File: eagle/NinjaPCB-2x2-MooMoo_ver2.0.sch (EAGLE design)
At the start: 75 parts, among them IC1 ANALOGSW_AD_SOT23-6, IC2 NAU7802, Q1 IRLB3813PBF, Q2 CJ2302, Q3 CJ2302, Q4 S9013, Q5 S9013, Q6 S9013, T1 TPTP20R, T2 TPTP20R, T3 TPTP20R, T4 TPTP20R, T5 TPTP20R, T6 TPTP20R, T7 TPTP20R

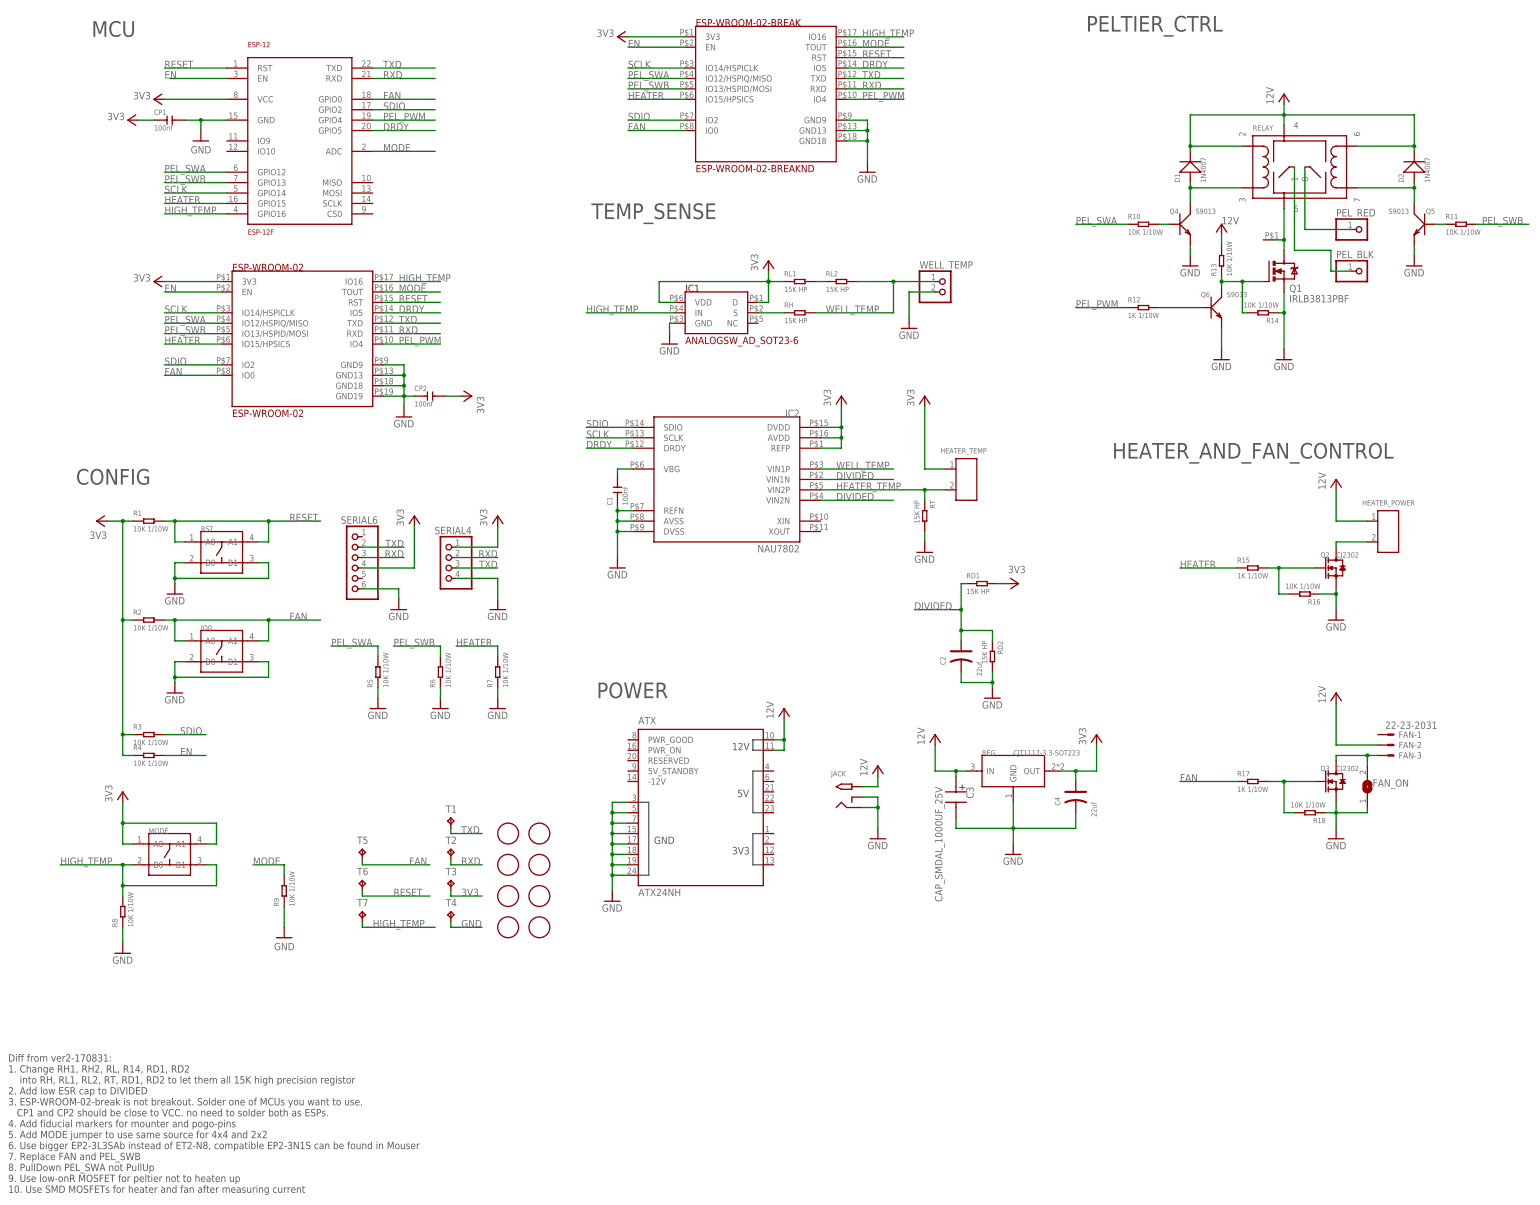
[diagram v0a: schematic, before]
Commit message: panelized NinNin
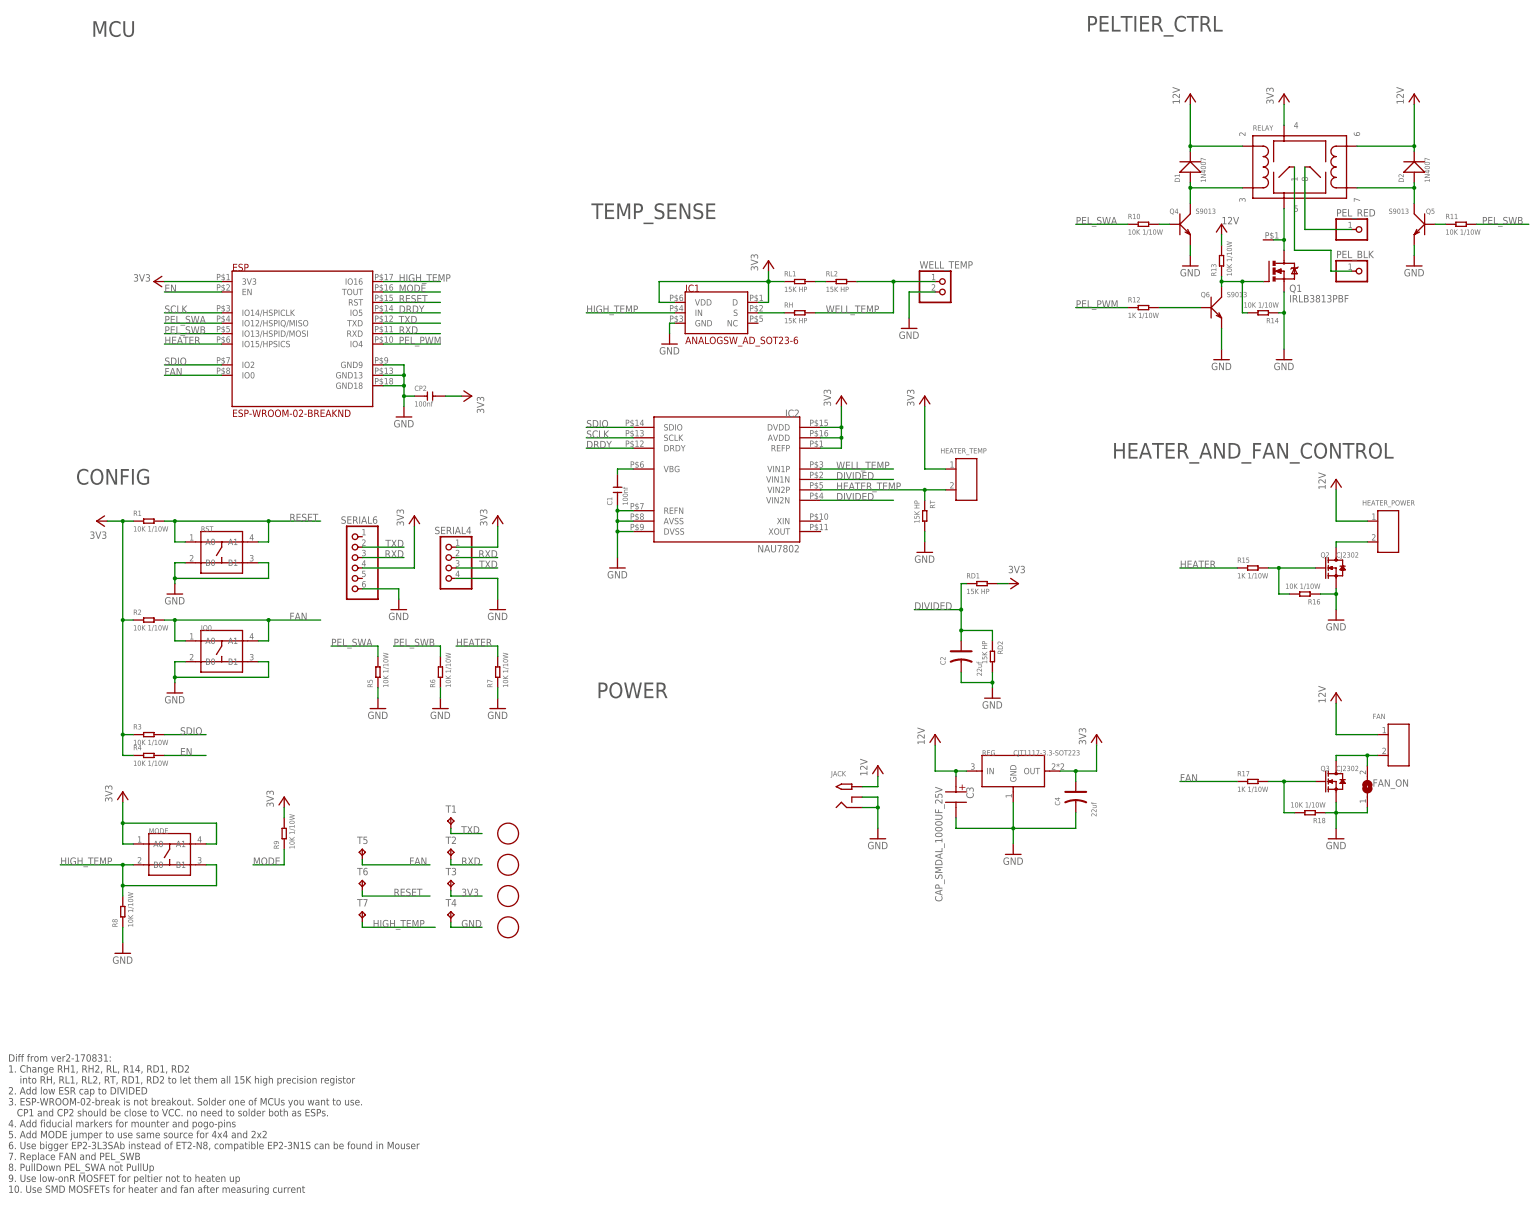
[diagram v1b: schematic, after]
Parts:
- removed ATX: ATX24NH, PCR-Connector:ATX24NH
- removed CP1: 100nf, Seeed-Capacitor:CERAMIC-100NF-50V-10%-X7R(0603)
- removed ESP-12: ESP-12F, Seeed-OPL-2017-01-Sensor-camilo:ESP-12F
- removed ESP-WROOM-02: ESP-WROOM-02, PCR-Module:ESP-WROOM-02
- removed ESP-WROOM-02-BREAK: ESP-WROOM-02-BREAKND, PCR-Module:ESP-WROOM-02-BREAKND
- removed U$10, U$7, U$8, U$9: FIDUCIAL, adafruit:FIDUCIAL
- added ESP: ESP-WROOM-02-BREAKND, PCR-Module:ESP-WROOM-02-BREAKND
- FAN: value 22-23-2031 -> (none); device con-molex:22-23-2031 -> Seeed-Connector:SCREW-TERMINAL-GREEN(2P-3.5)
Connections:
- new net N$9: D1.-, RELAY.2
- net 12V: now also FAN.1; no longer ATX.12V_10, ATX.12V_11, D1.-, FAN-2.S, RELAY.2, RELAY.4
- net 3V3: now also ESP.3V3, R9.2, RELAY.4; no longer CP1.1, ESP-12.VCC, ESP-WROOM-02-BREAK.3V3, ESP-WROOM-02.3V3
- net DRDY: now also ESP.IO5; no longer ESP-12.GPIO5, ESP-WROOM-02-BREAK.IO5, ESP-WROOM-02.IO5
- net EN: now also ESP.EN; no longer ESP-12.EN, ESP-WROOM-02-BREAK.EN, ESP-WROOM-02.EN
- net FAN: now also ESP.IO0; no longer ESP-12.GPIO0, ESP-WROOM-02-BREAK.IO0, ESP-WROOM-02.IO0
- net GND: now also ESP.GND13, ESP.GND18, ESP.GND9; no longer ATX.GND15, ATX.GND17, ATX.GND18, ATX.GND19, ATX.GND24, ATX.GND3, ATX.GND5, ATX.GND7, CP1.2, ESP-12.GND, ESP-WROOM-02-BREAK.GND13, ESP-WROOM-02-BREAK.GND18, ESP-WROOM-02-BREAK.GND9, ESP-WROOM-02.GND13, ESP-WROOM-02.GND18, ESP-WROOM-02.GND19, ESP-WROOM-02.GND9, R9.1
- net HEATER: now also ESP.IO15/HPSICS; no longer ESP-12.GPIO15, ESP-WROOM-02-BREAK.IO15/HPSICS, ESP-WROOM-02.IO15/HPSICS
- net HIGH_TEMP: now also ESP.IO16; no longer ESP-12.GPIO16, ESP-WROOM-02-BREAK.IO16, ESP-WROOM-02.IO16
- net MODE: now also ESP.TOUT, R9.1; no longer ESP-12.ADC, ESP-WROOM-02-BREAK.TOUT, ESP-WROOM-02.TOUT, R9.2
- net N$4: now also FAN.2; no longer FAN-3.S
- net PEL_PWM: now also ESP.IO4; no longer ESP-12.GPIO4, ESP-WROOM-02-BREAK.IO4, ESP-WROOM-02.IO4
- net PEL_SWA: now also ESP.IO12/HSPIQ/MISO; no longer ESP-12.GPIO12, ESP-WROOM-02-BREAK.IO12/HSPIQ/MISO, ESP-WROOM-02.IO12/HSPIQ/MISO
- net PEL_SWB: now also ESP.IO13/HSPID/MOSI; no longer ESP-12.GPIO13, ESP-WROOM-02-BREAK.IO13/HSPID/MOSI, ESP-WROOM-02.IO13/HSPID/MOSI
- net RESET: now also ESP.RST; no longer ESP-12.RST, ESP-WROOM-02-BREAK.RST, ESP-WROOM-02.RST
- net RXD: now also ESP.RXD; no longer ESP-12.RXD, ESP-WROOM-02-BREAK.RXD, ESP-WROOM-02.RXD
- net SCLK: now also ESP.IO14/HSPICLK; no longer ESP-12.GPIO14, ESP-WROOM-02-BREAK.IO14/HSPICLK, ESP-WROOM-02.IO14/HSPICLK
- net SDIO: now also ESP.IO2; no longer ESP-12.GPIO2, ESP-WROOM-02-BREAK.IO2, ESP-WROOM-02.IO2
- net TXD: now also ESP.TXD; no longer ESP-12.TXD, ESP-WROOM-02-BREAK.TXD, ESP-WROOM-02.TXD
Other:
- moved on the sheet: R9

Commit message: prepare for order
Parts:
- removed C3: CAP_SMDAL_1000UF_25V, Seeed-OPL-2017-01-Capacitor-akita:CAP_SMDAL_1000UF_25V
- removed C4: 22uf, Seeed-Capacitor:TANTALUM-SMD-22UF-16V(AVX-B)
- removed CP2: 100nf, Seeed-Capacitor:CERAMIC-100NF-50V-10%-X7R(0603)
- added C5: 22uf, Seeed-Capacitor:TANTALUM-SMD-22UF-16V(AVX-B)
- added C6: 1uf, Seeed-Capacitor:CERAMIC-1UF-25V-10%-X7R(0603)
- added CP: 100nf, Seeed-Capacitor:CERAMIC-100NF-50V-10%-X7R(0603)
- added MONITOR: (no value), pinhead:PINHD-1X3
- added R19: 10K 1/10W, Seeed-Resistor:SMD-RES-10K-5%-1/10W(0603)
- REG: value CJT1117-3.3-SOT223 -> RT7258QW; device Seeed-IC:PMIC-CJT1117-3.3(SOT223) -> PCR-IC:RT7258QW
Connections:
- new net N$10: C6.2, MONITOR.1, R19.1, REG.VCC
- new net N$11: MONITOR.2, R19.2, REG.PGOOD
- new net N$12: MONITOR.3, REG.EN/SYNC
- net 12V: now also C5.+, REG.VIN4, REG.VIN5, REG.VIN6; no longer C3.P$P, REG.IN
- net 3V3: now also CP.2; no longer C4.+, CP2.2, REG.OUT
- net GND: now also C5.-, C6.1, CP.1, REG.GND14, REG.GND15; no longer C3.P$M, C4.-, CP2.1, REG.GND
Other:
- moved on the sheet: C1, C2, ESP, HEATER_TEMP, IC1, IC2, JACK, RD1, RD2, RH, RL1, RL2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

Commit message: ordered
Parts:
- added C3: 1uf, Seeed-Capacitor:CERAMIC-1UF-25V-10%-X7R(0603)
- added C4, C7, C8, C9: 22uf, Seeed-Capacitor:TANTALUM-SMD-22UF-16V(AVX-B)
- added HEATSINK1: HEAT111PB015, PCR-Connector:HEAT111PB015
- added L1: SFT1240, inductors:SFT1240
- added Q7: IRLB3813PBF, transistor-power:IRF520
- added R20: 10K 1/10W, Seeed-Resistor:SMD-RES-10K-5%-1/10W(0603)
- added R21: 68K(62K is better), Seeed-Resistor:SMD-RES-30K-5%-1/10W(0603)
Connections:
- new net FB: R20.2, R21.1, REG.FB
- new net N$13: C3.2, REG.BOOT
- new net N$14: C3.1, HEATSINK1.P$1, L1.1, Q7.D, REG.SW10, REG.SW8, REG.SW9
- new net N$15: Q7.G, REG.BG
- net 3V3: now also C4.+, C7.+, C8.+, C9.+, L1.2, R21.2
- net GND: now also C4.-, C7.-, C8.-, C9.-, Q7.S, R20.1
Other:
- moved on the sheet: FAN, FAN_ON, HEATER_POWER, Q2, Q3, R15, R16, R17, R18
